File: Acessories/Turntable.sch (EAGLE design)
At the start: 31 parts, among them IC1 7812TV, IC2 7805TV, J1 HEADER4, M1 ARDUINO-NANO-3.0, U2 A4988, X1 MKDSN1,5/4-5,08

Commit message: Add files via upload
Updated turntable design, added 3.5mm connector for stepper motor and direct control of the stepping levels
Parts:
- removed J1: HEADER4, GJR:HEADER4
- added X2: 1751248, con-phoenix-350:1751248
- added X3: 1751264, con-phoenix-350:1751264
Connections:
- net +5V: now also JP1.2; no longer JP1.3
- net 1A: now also X3-3.K; no longer J1-2.S
- net 1B: now also X3-4.K; no longer J1-1.S
- net 2A: now also X3-1.K; no longer J1-4.S
- net 2B: now also X3-2.K; no longer J1-3.S
- net GND: now also JP1.3; no longer JP1.2
- net TRACK1: now also X2-1.K
- net TRACK2: now also X2-2.K
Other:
- moved on the sheet: X1-2
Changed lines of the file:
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@@
 <?xml version="1.0" encoding="utf-8"?>
 <!DOCTYPE eagle SYSTEM "eagle.dtd">
-<eagle version="9.4.0">
+<eagle version="9.4.2">
 <drawing>
 <settings>
@@
 <setting verticaltext="up"/>
 </settings>
-<grid distance="0.05" unitdist="inch" unit="inch" style="lines" multiple="1" display="no" altdistance="0.01" altunitdist="inch" altunit="inch"/>
+<grid distance="0.1" unitdist="inch" unit="inch" style="lines" multiple="1" display="no" altdistance="0.01" altunitdist="inch" altunit="inch"/>
 <layers>
 <layer number="1" name="Top" color="4" fill="1" visible="no" active="no"/>
@@
 <part name="M1" library="diy-modules" deviceset="ARDUINO-NANO-3.0" device=""/>
 <part name="U2" library="GJR" deviceset="A4988" device=""/>
-<part name="J1" library="GJR" deviceset="HEADER4" device=""/>
 <part name="GND9" library="supply1" deviceset="GND" device=""/>
 <part name="GND10" library="supply1" deviceset="GND" device=""/>
@@
 <part name="IC1" library="linear" library_urn="urn:adsk.eagle:library:262" deviceset="78*" device="TV" package3d_urn="urn:adsk.eagle:package:16417/2" technology="12"/>
 <part name="IC2" library="linear" library_urn="urn:adsk.eagle:library:262" deviceset="78*" device="TV" package3d_urn="urn:adsk.eagle:package:16417/2" technology="05"/>
+<part name="X3" library="con-phoenix-350" deviceset="1751264" device=""/>
+<part name="X2" library="con-phoenix-350" library_urn="urn:adsk.eagle:library:174" deviceset="1751248" device="" package3d_urn="urn:adsk.eagle:package:9395/1"/>
 </parts>
 <sheets>
@@
 <attribute name="NAME" x="17.399" y="144.018" size="1.778" layer="95" rot="R90"/>
 </instance>
-<instance part="X1" gate="-2" x="10.16" y="140.97" smashed="yes" rot="R90">
-<attribute name="NAME" x="11.049" y="144.018" size="1.778" layer="95" rot="R90"/>
+<instance part="X1" gate="-2" x="8.89" y="140.97" smashed="yes" rot="R90">
+<attribute name="NAME" x="9.779" y="144.018" size="1.778" layer="95" rot="R90"/>
 </instance>
 <instance part="X1" gate="-3" x="35.56" y="162.56" smashed="yes" rot="R180">
@@
 </instance>
 <instance part="U2" gate="G$1" x="168.91" y="97.79" smashed="yes"/>
-<instance part="J1" gate="-1" x="138.43" y="102.87" smashed="yes" rot="R180">
-<attribute name="NAME" x="135.89" y="103.632" size="1.524" layer="95" rot="R180"/>
-</instance>
-<instance part="J1" gate="-2" x="138.43" y="100.33" smashed="yes" rot="R180">
-<attribute name="NAME" x="135.89" y="101.092" size="1.524" layer="95" rot="R180"/>
-</instance>
-<instance part="J1" gate="-3" x="138.43" y="92.71" smashed="yes" rot="R180">
-<attribute name="NAME" x="135.89" y="93.472" size="1.524" layer="95" rot="R180"/>
-</instance>
-<instance part="J1" gate="-4" x="138.43" y="95.25" smashed="yes" rot="R180">
-<attribute name="NAME" x="135.89" y="96.012" size="1.524" layer="95" rot="R180"/>
-</instance>
 <instance part="GND9" gate="1" x="166.37" y="72.39" smashed="yes">
 <attribute name="VALUE" x="163.83" y="69.85" size="1.778" layer="96"/>
@@
 <attribute name="NAME" x="105.41" y="168.275" size="1.778" layer="95"/>
 <attribute name="VALUE" x="105.41" y="165.735" size="1.778" layer="96"/>
+</instance>
+<instance part="X2" gate="-1" x="21.59" y="140.97" smashed="yes" rot="R90">
+<attribute name="NAME" x="22.479" y="142.24" size="1.778" layer="95" rot="R90"/>
+<attribute name="VALUE" x="22.479" y="154.94" size="1.778" layer="96" rot="R90"/>
+</instance>
+<instance part="X2" gate="-2" x="12.7" y="140.97" smashed="yes" rot="R90">
+<attribute name="NAME" x="13.589" y="142.24" size="1.778" layer="95" rot="R90"/>
+<attribute name="VALUE" x="13.589" y="154.94" size="1.778" layer="96" rot="R90"/>
+</instance>
+<instance part="X3" gate="-1" x="138.43" y="95.25" smashed="yes" rot="R180">
+<attribute name="NAME" x="137.16" y="96.139" size="1.778" layer="95" rot="R180"/>
+<attribute name="VALUE" x="124.46" y="96.139" size="1.778" layer="96" rot="R180"/>
+</instance>
+<instance part="X3" gate="-3" x="138.43" y="100.33" smashed="yes" rot="R180">
+<attribute name="NAME" x="137.16" y="101.219" size="1.778" layer="95" rot="R180"/>
+<attribute name="VALUE" x="124.46" y="101.219" size="1.778" layer="96" rot="R180"/>
+</instance>
+<instance part="X3" gate="-4" x="138.43" y="102.87" smashed="yes" rot="R180">
+<attribute name="NAME" x="137.16" y="103.759" size="1.778" layer="95" rot="R180"/>
+<attribute name="VALUE" x="124.46" y="103.759" size="1.778" layer="96" rot="R180"/>
+</instance>
+<instance part="X3" gate="-2" x="138.43" y="92.71" smashed="yes" rot="R180">
+<attribute name="NAME" x="137.16" y="93.599" size="1.778" layer="95" rot="R180"/>
+<attribute name="VALUE" x="124.46" y="93.599" size="1.778" layer="96" rot="R180"/>
 </instance>
 </instances>
@@
 </segment>
 <segment>
-<pinref part="GND1" gate="1" pin="GND"/>
-<wire x1="40.64" y1="77.47" x2="40.64" y2="71.12" width="0.1524" layer="91"/>
-<pinref part="JP1" gate="A" pin="2"/>
-<wire x1="34.29" y1="77.47" x2="40.64" y2="77.47" width="0.1524" layer="91"/>
-</segment>
-<segment>
 <pinref part="GND7" gate="1" pin="GND"/>
 <pinref part="S1" gate="1" pin="O"/>
 <wire x1="129.54" y1="53.34" x2="133.35" y2="53.34" width="0.1524" layer="91"/>
 <wire x1="133.35" y1="53.34" x2="133.35" y2="45.72" width="0.1524" layer="91"/>
+</segment>
+<segment>
+<pinref part="JP1" gate="A" pin="3"/>
+<pinref part="GND1" gate="1" pin="GND"/>
+<wire x1="34.29" y1="74.93" x2="40.64" y2="74.93" width="0.1524" layer="91"/>
+<wire x1="40.64" y1="74.93" x2="40.64" y2="71.12" width="0.1524" layer="91"/>
 </segment>
 </net>
@@
 </segment>
 <segment>
-<pinref part="JP1" gate="A" pin="3"/>
 <pinref part="P+1" gate="1" pin="+5V"/>
-<wire x1="34.29" y1="74.93" x2="43.18" y2="74.93" width="0.1524" layer="91"/>
-<wire x1="43.18" y1="74.93" x2="43.18" y2="83.82" width="0.1524" layer="91"/>
+<pinref part="JP1" gate="A" pin="2"/>
+<wire x1="43.18" y1="77.47" x2="43.18" y2="83.82" width="0.1524" layer="91"/>
+<wire x1="34.29" y1="77.47" x2="43.18" y2="77.47" width="0.1524" layer="91"/>
 </segment>
 <segment>
@@
 <wire x1="29.21" y1="100.33" x2="24.13" y2="100.33" width="0.1524" layer="91"/>
 <wire x1="24.13" y1="100.33" x2="16.51" y2="100.33" width="0.1524" layer="91"/>
-<wire x1="16.51" y1="100.33" x2="10.16" y2="100.33" width="0.1524" layer="91"/>
-<wire x1="10.16" y1="100.33" x2="10.16" y2="129.54" width="0.1524" layer="91"/>
+<wire x1="16.51" y1="100.33" x2="8.89" y2="100.33" width="0.1524" layer="91"/>
+<wire x1="8.89" y1="100.33" x2="8.89" y2="129.54" width="0.1524" layer="91"/>
 <label x="8.89" y="127" size="1.778" layer="95" rot="R90"/>
 <junction x="16.51" y="100.33"/>
 <pinref part="X1" gate="-2" pin="KL"/>
 <pinref part="D1" gate="G$1" pin="A"/>
-<wire x1="10.16" y1="129.54" x2="10.16" y2="138.43" width="0.1524" layer="91"/>
+<wire x1="8.89" y1="129.54" x2="8.89" y2="138.43" width="0.1524" layer="91"/>
 <wire x1="24.13" y1="105.41" x2="24.13" y2="100.33" width="0.1524" layer="91"/>
 <junction x="24.13" y="100.33"/>
-<wire x1="34.29" y1="129.54" x2="10.16" y2="129.54" width="0.1524" layer="91"/>
-<junction x="10.16" y="129.54"/>
+<wire x1="34.29" y1="129.54" x2="12.7" y2="129.54" width="0.1524" layer="91"/>
+<junction x="8.89" y="129.54"/>
 <label x="34.29" y="129.54" size="1.778" layer="95" xref="yes"/>
+<wire x1="12.7" y1="129.54" x2="8.89" y2="129.54" width="0.1524" layer="91"/>
+<wire x1="12.7" y1="138.43" x2="12.7" y2="129.54" width="0.1524" layer="91"/>
+<junction x="12.7" y="129.54"/>
+<pinref part="X2" gate="-2" pin="K"/>
 </segment>
 </net>
@@
 <segment>
 <pinref part="R1" gate="G$1" pin="2"/>
-<wire x1="16.51" y1="128.27" x2="16.51" y2="138.43" width="0.1524" layer="91"/>
+<wire x1="16.51" y1="128.27" x2="16.51" y2="134.62" width="0.1524" layer="91"/>
 <label x="16.51" y="129.54" size="1.778" layer="95" rot="R90"/>
 <pinref part="X1" gate="-1" pin="KL"/>
+<wire x1="16.51" y1="134.62" x2="16.51" y2="138.43" width="0.1524" layer="91"/>
+<wire x1="21.59" y1="138.43" x2="21.59" y2="134.62" width="0.1524" layer="91"/>
+<wire x1="21.59" y1="134.62" x2="16.51" y2="134.62" width="0.1524" layer="91"/>
+<junction x="16.51" y="134.62"/>
+<pinref part="X2" gate="-1" pin="K"/>
 </segment>
 </net>
@@
 <pinref part="U2" gate="G$1" pin="1B"/>
 <wire x1="151.13" y1="102.87" x2="140.97" y2="102.87" width="0.1524" layer="91"/>
-<pinref part="J1" gate="-1" pin="S"/>
 <label x="142.24" y="102.87" size="1.27" layer="95"/>
+<pinref part="X3" gate="-4" pin="K"/>
 </segment>
 </net>
@@
 <pinref part="U2" gate="G$1" pin="1A"/>
 <wire x1="151.13" y1="100.33" x2="140.97" y2="100.33" width="0.1524" layer="91"/>
-<pinref part="J1" gate="-2" pin="S"/>
 <label x="142.24" y="100.33" size="1.27" layer="95"/>
+<pinref part="X3" gate="-3" pin="K"/>
 </segment>
 </net>
@@
 <pinref part="U2" gate="G$1" pin="2A"/>
 <wire x1="151.13" y1="95.25" x2="140.97" y2="95.25" width="0.1524" layer="91"/>
-<pinref part="J1" gate="-4" pin="S"/>
 <label x="142.24" y="95.25" size="1.27" layer="95"/>
+<pinref part="X3" gate="-1" pin="K"/>
 </segment>
 </net>
@@
 <pinref part="U2" gate="G$1" pin="2B"/>
 <wire x1="151.13" y1="92.71" x2="140.97" y2="92.71" width="0.1524" layer="91"/>
-<pinref part="J1" gate="-3" pin="S"/>
 <label x="142.24" y="92.71" size="1.27" layer="95"/>
-</segment>
-</net>
+<pinref part="X3" gate="-2" pin="K"/>
+</segment>
+</net>

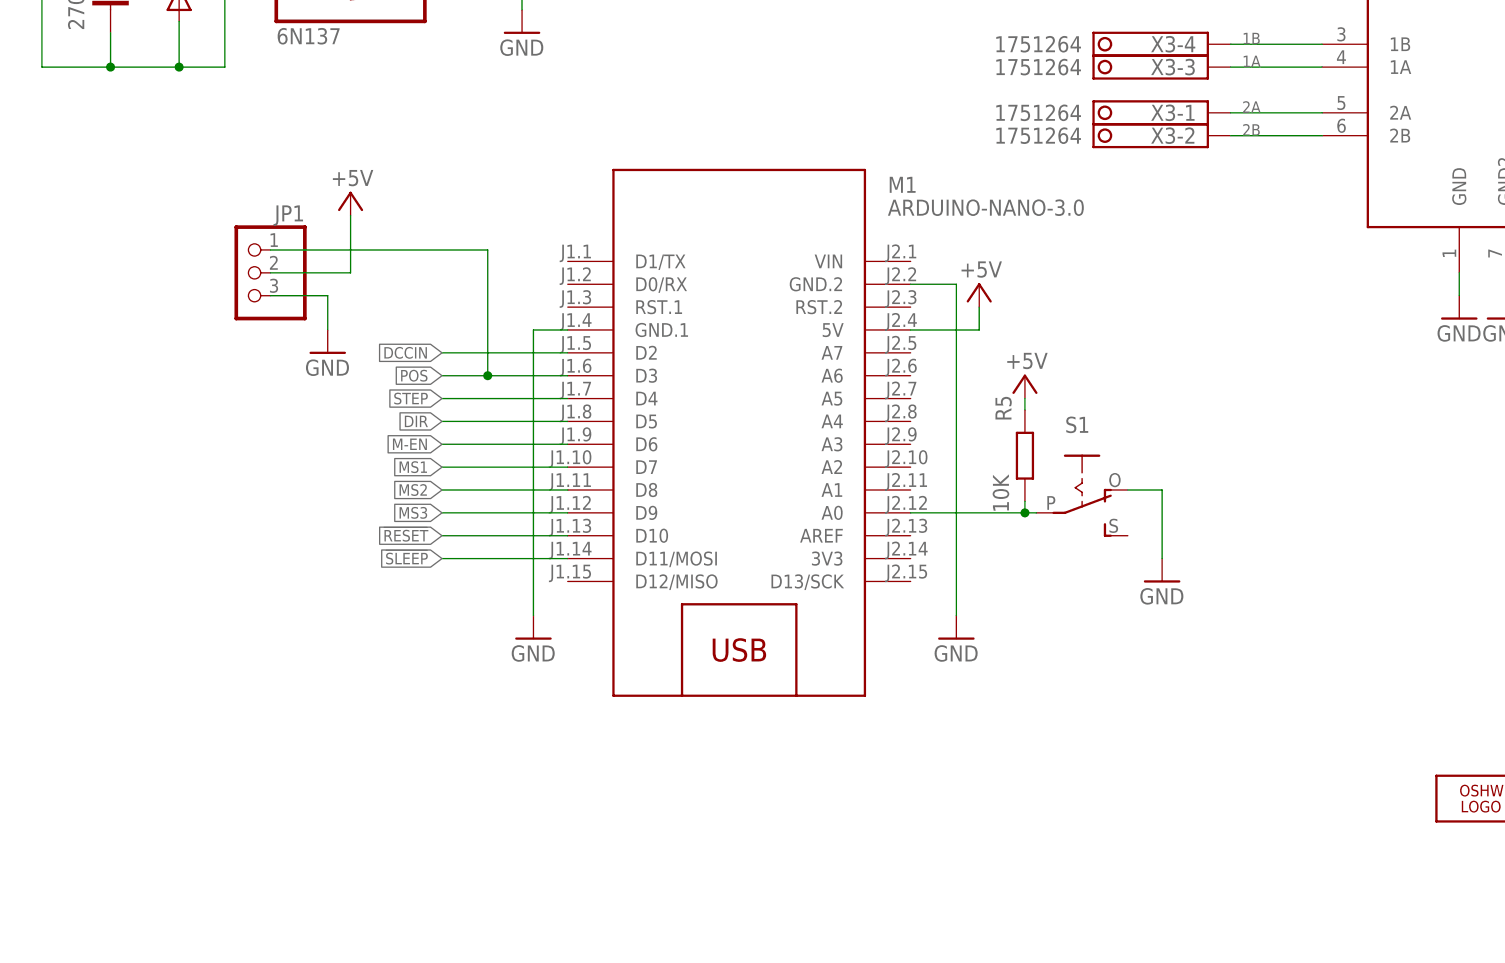
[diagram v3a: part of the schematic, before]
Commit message: Add files via upload
added 2 more sensor inputs to enable multiple sensing locations. Intended home, first engine, last engine
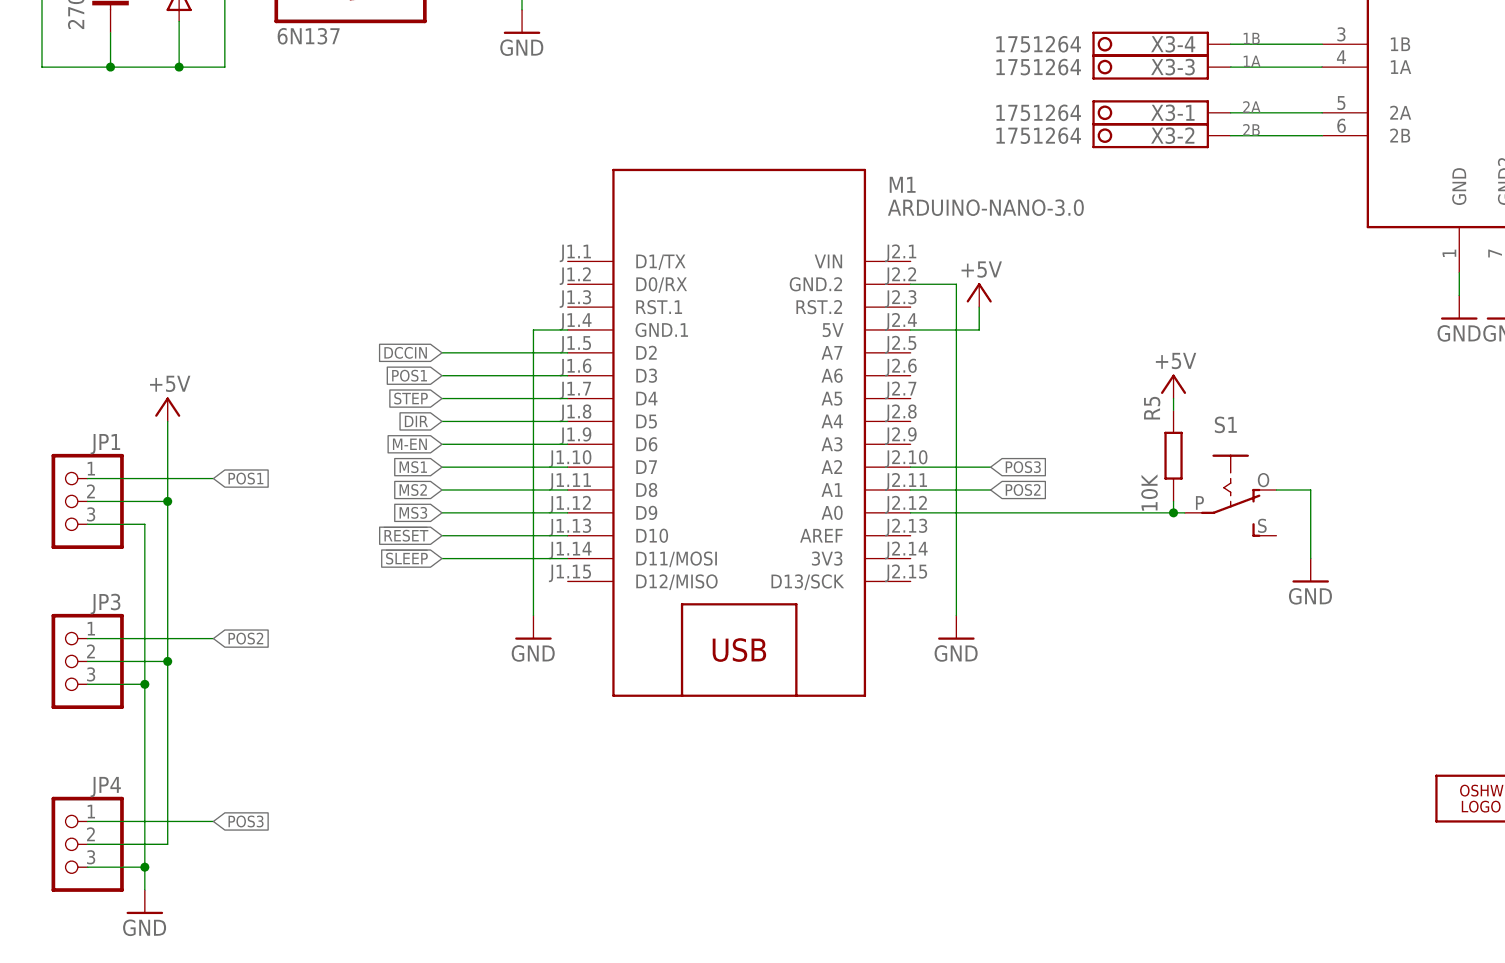
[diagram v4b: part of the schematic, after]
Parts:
- added JP3, JP4: (no value), adafruit:PINHD-1X3
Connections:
- net POS renamed POS1
- new net POS2: JP3.1, M1.A1
- new net POS3: JP4.1, M1.A2
- net +5V: now also JP3.2, JP4.2
- net GND: now also JP3.3, JP4.3
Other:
- moved on the sheet: JP1, R5, S1
